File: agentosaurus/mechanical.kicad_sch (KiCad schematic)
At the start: 4 parts

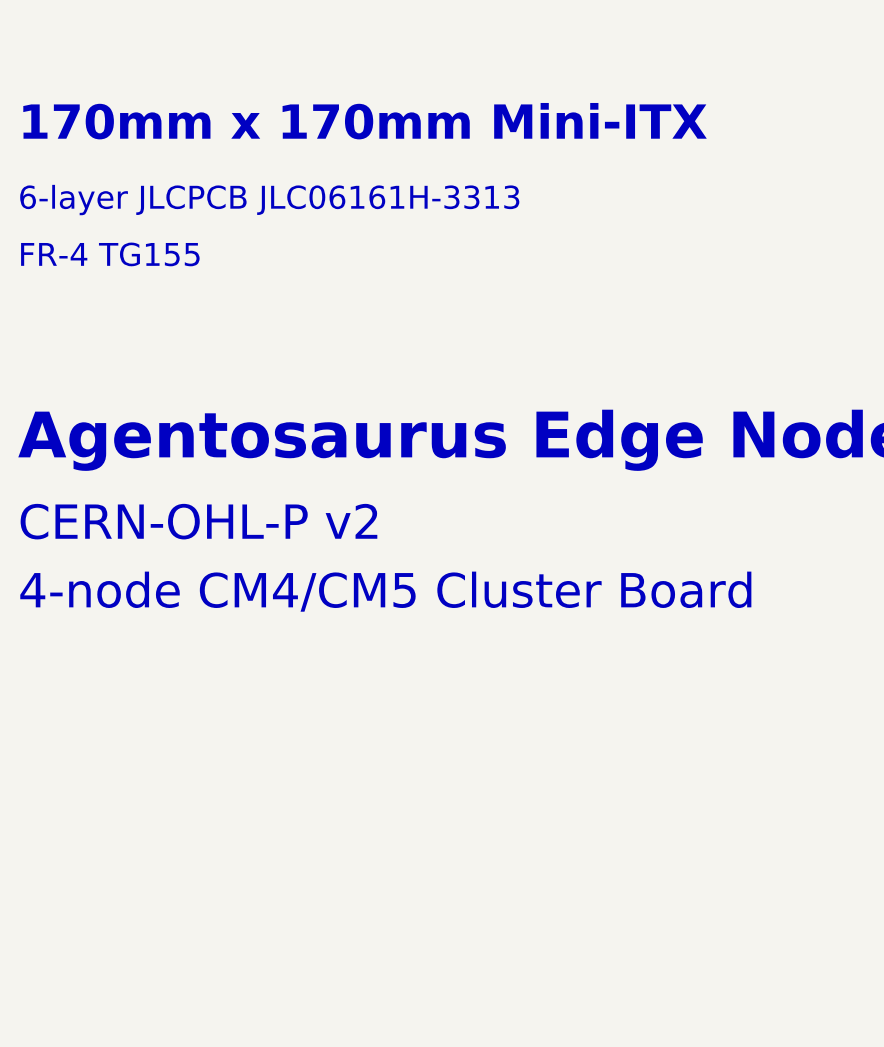
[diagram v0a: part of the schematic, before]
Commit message: Add passive components to all schematic sheets
- power.kicad_sch: Fix D1 catch diode rotation (cathode→SW), remove
  incorrect COMP-to-output wire, add all TPS54360 application circuit
  passives (CIN1/2, CBOOT, L1, COUT1-3, R_EN1/2, R_RT, R_FB1/2,
  R_COMP, C_COMP) and AMS1117 caps (CIN_LDO, COUT_LDO)
- bmc.kicad_sch: Add USB-C CC pull-downs (R1/R2 5.1k), ESP32 reset
  circuit (R3 10k + C9 1uF), decoupling caps for ESP32 (C10/C11),
  UART mux (C12), USB mux (C13/C14), WS2812B (C15-C18), I2C
  pull-ups (R4/R5 4.7k)
- cm4-slot.kicad_sch: Add magnetics center-tap decoupling (C1-C4
  100nF) and power rail decoupling (C5-C8)
- ethernet-switch.kicad_sch: Add crystal load caps (C1/C2 22pF),
  3.3V decoupling (C3-C10), 1.0V core decoupling (C11-C16),
  Slot 2 Ethernet wiring to RTL8367S
- mechanical.kicad_sch: Add PCB stackup, impedance control, and
  via specifications

https://claude.ai/code/session_01UhhXLgEHsAy83XEALyNrDb
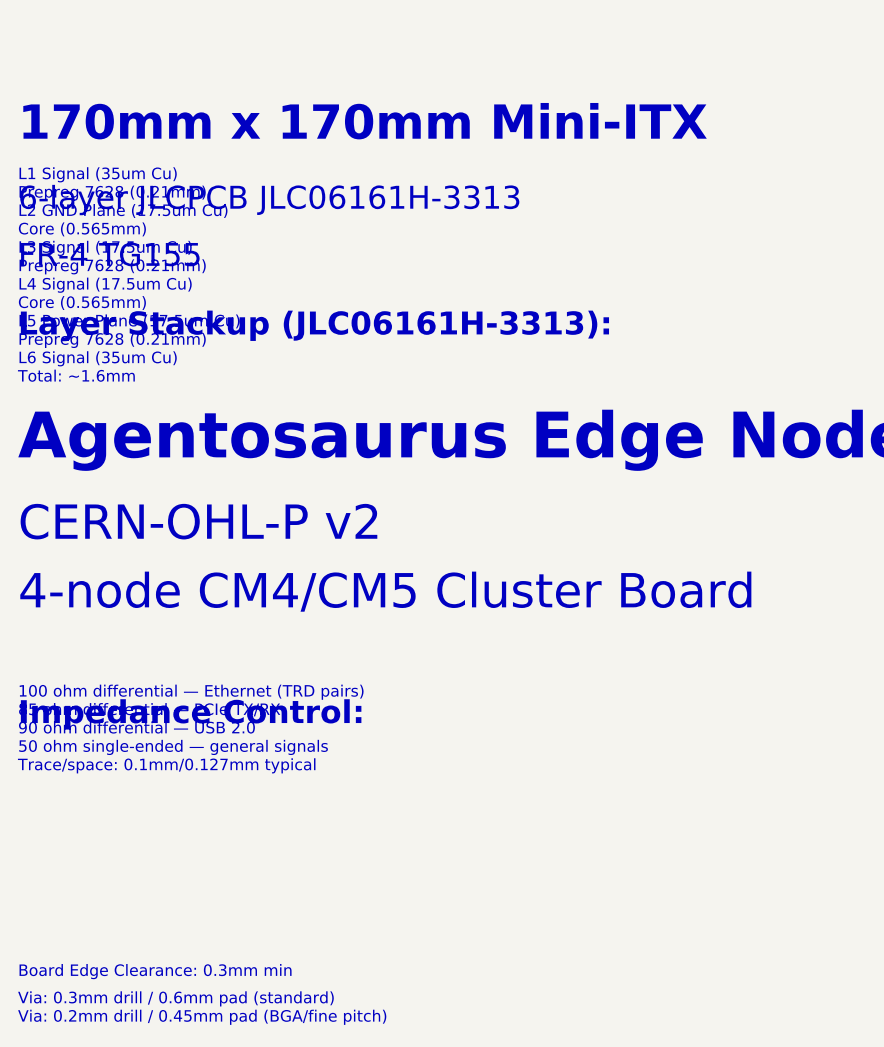
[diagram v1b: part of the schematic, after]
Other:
- note added: "100 ohm differential — Ethernet (TRD pairs) 85 ohm differential — PCIe TX/RX 90 ohm differential — USB 2.0 50 ohm single-ended — general signals Trace/space: 0.1mm/0.127mm typical"
- note added: "Board Edge Clearance: 0.3mm min"
- note added: "Impedance Control:"
- note added: "L1 Signal (35um Cu) Prepreg 7628 (0.21mm) L2 GND Plane (17.5um Cu) Core (0.565mm) L3 Signal (17.5um Cu) Prepreg 7628 (0.21mm) L4 Signal (17.5um Cu) Core (0.565mm) L5 Power Plane (17.5um Cu) Prepreg 7628 (0.21mm) L6 Signal (35um Cu) Total: ~1.6mm"
- note added: "Layer Stackup (JLC06161H-3313):"
- note added: "Via: 0.3mm drill / 0.6mm pad (standard) Via: 0.2mm drill / 0.45mm pad (BGA/fine pitch)"
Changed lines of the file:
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@@
     (effects (font (size 2.54 2.54)) (justify left bottom))
+  )
+  (text "Layer Stackup (JLC06161H-3313):" (at 50.8 121.92 0)
+    (effects (font (size 2.54 2.54) bold) (justify left bottom))
+  )
+  (text "L1 Signal (35um Cu)\nPrepreg 7628 (0.21mm)\nL2 GND Plane (17.5um Cu)\nCore (0.565mm)\nL3 Signal (17.5um Cu)\nPrepreg 7628 (0.21mm)\nL4 Signal (17.5um Cu)\nCore (0.565mm)\nL5 Power Plane (17.5um Cu)\nPrepreg 7628 (0.21mm)\nL6 Signal (35um Cu)\nTotal: ~1.6mm" (at 50.8 127 0)
+    (effects (font (size 1.27 1.27)) (justify left bottom))
+  )
+  (text "Impedance Control:" (at 50.8 165.1 0)
+    (effects (font (size 2.54 2.54) bold) (justify left bottom))
+  )
+  (text "100 ohm differential — Ethernet (TRD pairs)\n85 ohm differential — PCIe TX/RX\n90 ohm differential — USB 2.0\n50 ohm single-ended — general signals\nTrace/space: 0.1mm/0.127mm typical" (at 50.8 170.18 0)
+    (effects (font (size 1.27 1.27)) (justify left bottom))
+  )
+  (text "Board Edge Clearance: 0.3mm min" (at 50.8 193.04 0)
+    (effects (font (size 1.27 1.27)) (justify left bottom))
+  )
+  (text "Via: 0.3mm drill / 0.6mm pad (standard)\nVia: 0.2mm drill / 0.45mm pad (BGA/fine pitch)" (at 50.8 198.12 0)
+    (effects (font (size 1.27 1.27)) (justify left bottom))
   )
   ;; ---------------------------------------------------------------
